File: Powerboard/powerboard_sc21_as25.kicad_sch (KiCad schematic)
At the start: 59 parts, among them J10 Conn_01x04_Male, J2 Conn_01x02_Male, J3 Conn_01x02_Male, J4 Conn_01x08_Male, J9 Conn_Coaxial, Q6 MMDT2222A, Q7 RSJ250P10TL, Q8 RSJ250P10TL, U1 LTC4412xS6, U2 SN65HVD230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

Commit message: update
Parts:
- removed TP1, TP10, TP11, TP12, TP13, TP2, TP26, TP27, TP3, TP4, TP5, TP6, TP7, TP8, TP9: TestPoint, TestPoint:TestPoint_Pad_D1.0mm, symbol Connector:TestPoint
- added C21: 160pF, Capacitor_SMD:C_0603_1608Metric, symbol Device:C_Small
- C17, C18, C2: value 1uF -> 1μF
- C28: value 220pF -> 220 pF
- R11, R4: value 10k -> 10kΩ
- R19, R21, R6, R8: value 470 -> 470Ω
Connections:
- net GND: now also U3.16 (IO27), C21.1
- net at R22.2, U2.1 (D): now also C21.2
- no-connect marks 22 -> 21

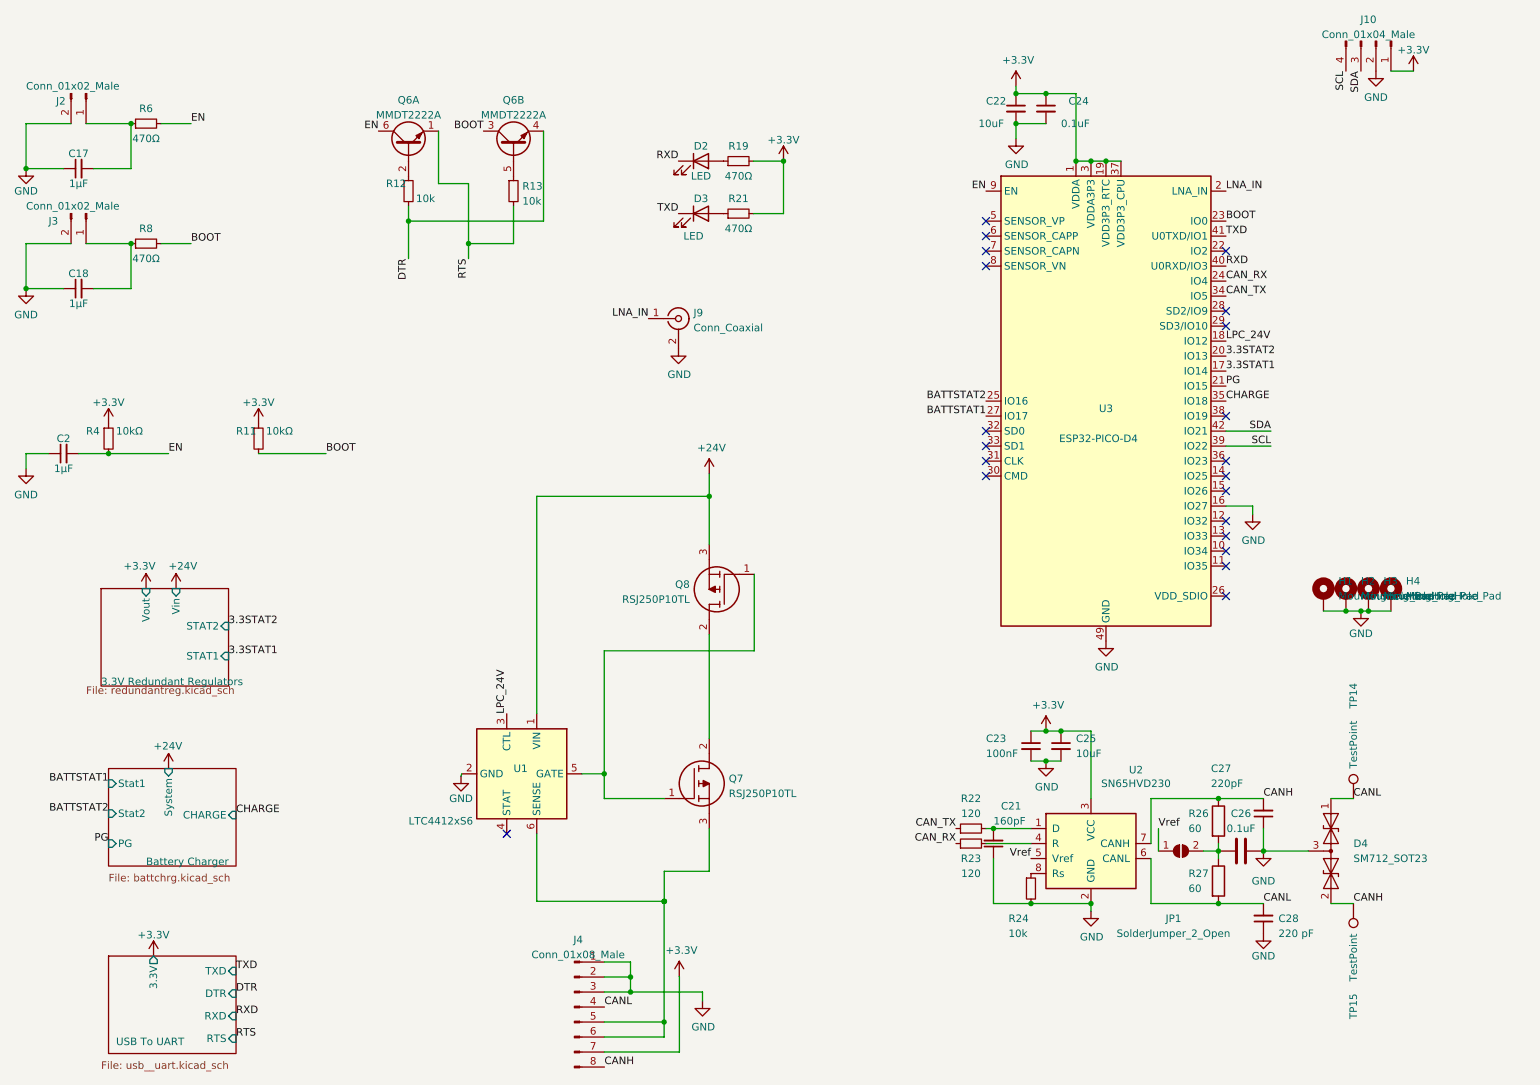
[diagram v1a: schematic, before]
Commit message: Changed some values and footprints since some went out of stock
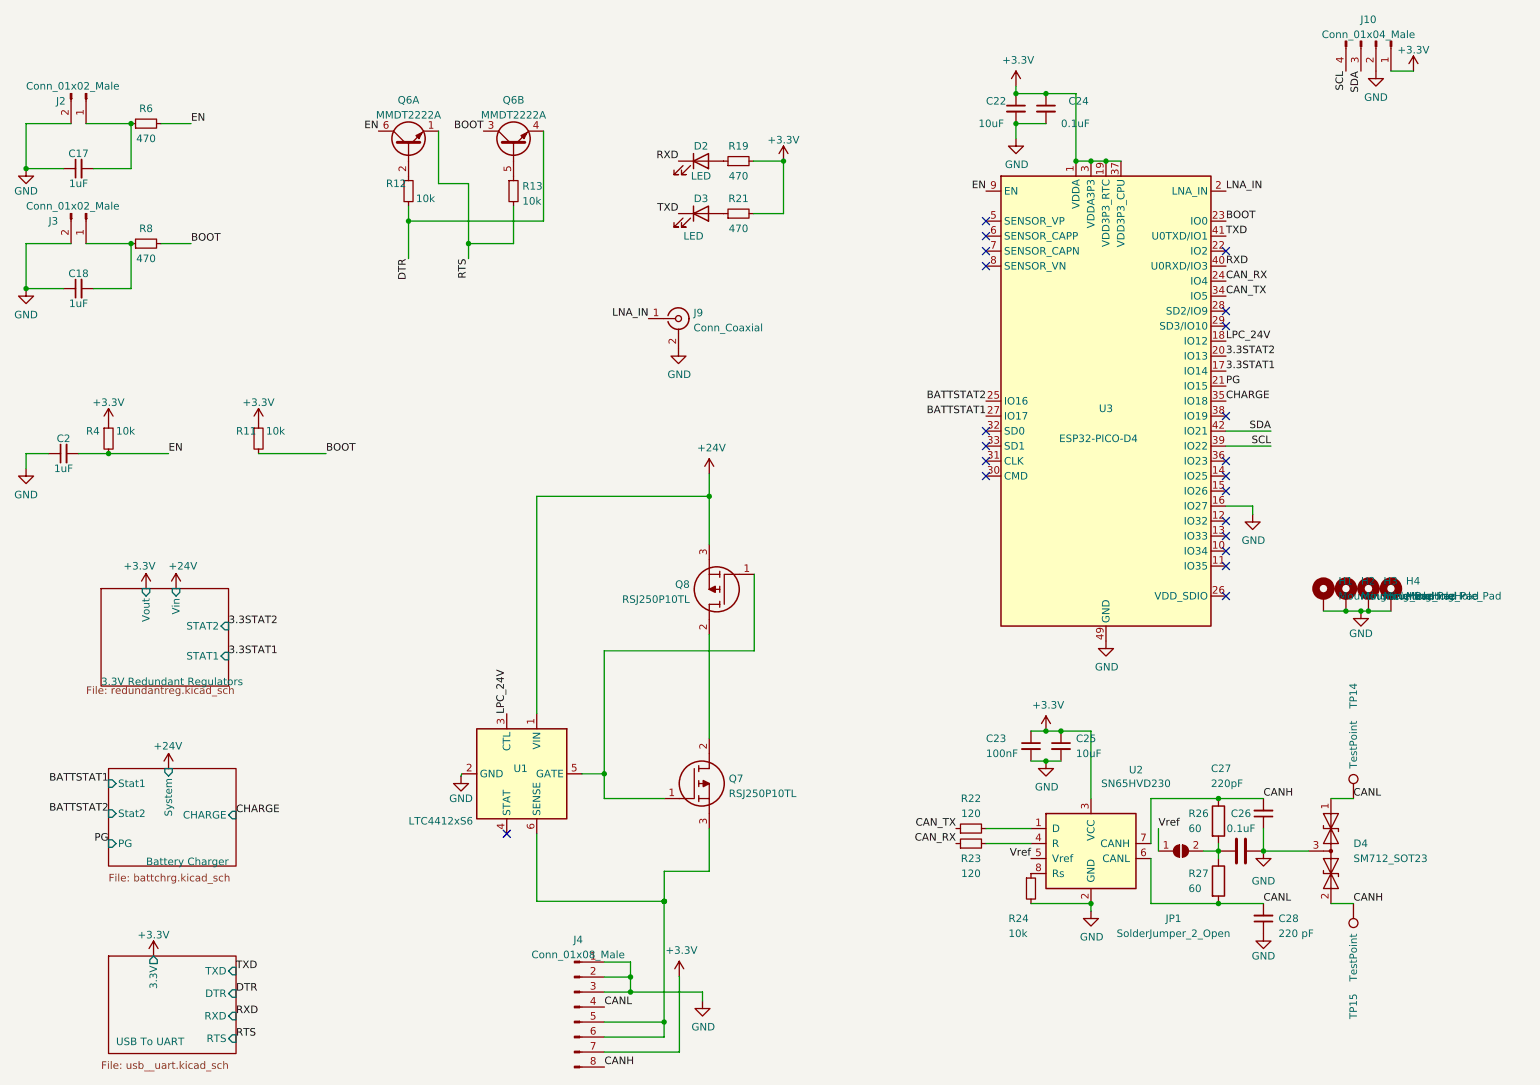
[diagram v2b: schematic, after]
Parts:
- removed C21: 160pF, Capacitor_SMD:C_0603_1608Metric, symbol Device:C_Small
- C17, C18, C2: value 1μF -> 1uF
- R11, R4: value 10kΩ -> 10k
- R19, R21, R6, R8: value 470Ω -> 470

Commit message: update
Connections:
- net LPC_24V: no longer U1.3 (CTL)
- net at Q7.3, U1.6 (SENSE): now also J4.5 (Pin_5), J4.6 (Pin_6)
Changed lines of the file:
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@@
   (junction (at 217.17 33.02) (diameter 0) (color 0 0 0 0)
   )
+  (junction (at 150.0124 146.9644) (diameter 0) (color 0 0 0 0)
+  )
   (junction (at 257.81 109.22) (diameter 0) (color 0 0 0 0)
   )
+  (junction (at 52.07 26.67) (diameter 0) (color 0 0 0 0)
+  )
+  (junction (at 109.22 46.99) (diameter 0) (color 0 0 0 0)
+  )
+  (junction (at 52.07 46.99) (diameter 0) (color 0 0 0 0)
+  )
+  (junction (at 243.84 149.86) (diameter 0) (color 0 0 0 0)
+  )
+  (junction (at 132.207 136.779) (diameter 0) (color 0 0 0 0)
+  )
+  (junction (at 136.652 173.736) (diameter 0) (color 0 0 0 0)
+  )
+  (junction (at 48.26 82.55) (diameter 0) (color 0 0 0 0)
+  )
+  (junction (at 236.22 149.86) (diameter 0) (color 0 0 0 0)
+  )
+  (junction (at 136.652 171.196) (diameter 0) (color 0 0 0 0)
+  )
+  (junction (at 212.09 33.02) (diameter 0) (color 0 0 0 0)
+  )
   (junction (at 142.3416 178.816) (diameter 0) (color 0 0 0 0)
   )
-  (junction (at 52.07 26.67) (diameter 0) (color 0 0 0 0)
-  )
-  (junction (at 109.22 46.99) (diameter 0) (color 0 0 0 0)
-  )
-  (junction (at 52.07 46.99) (diameter 0) (color 0 0 0 0)
-  )
-  (junction (at 142.3924 158.3944) (diameter 0) (color 0 0 0 0)
-  )
-  (junction (at 243.84 149.86) (diameter 0) (color 0 0 0 0)
-  )
-  (junction (at 132.207 136.779) (diameter 0) (color 0 0 0 0)
-  )
-  (junction (at 136.652 173.736) (diameter 0) (color 0 0 0 0)
-  )
-  (junction (at 48.26 82.55) (diameter 0) (color 0 0 0 0)
-  )
-  (junction (at 236.22 149.86) (diameter 0) (color 0 0 0 0)
-  )
-  (junction (at 136.652 171.196) (diameter 0) (color 0 0 0 0)
-  )
-  (junction (at 142.367 158.369) (diameter 0) (color 0 0 0 0)
-  )
-  (junction (at 212.09 33.02) (diameter 0) (color 0 0 0 0)
-  )
   (junction (at 99.06 43.18) (diameter 0) (color 0 0 0 0)
   )
@@
   )
   (junction (at 260.35 109.22) (diameter 0) (color 0 0 0 0)
-  )
-  (junction (at 142.3416 158.3944) (diameter 0) (color 0 0 0 0)
   )
   (junction (at 207.01 129.54) (diameter 0) (color 0 0 0 0)
@@
   (no_connect (at 196.85 45.72))
   (no_connect (at 237.49 88.9))
-  (no_connect (at 115.697 146.939))
+  (no_connect (at 115.7224 146.9644))
   (no_connect (at 237.49 60.96))
   (no_connect (at 237.49 76.2))
@@
     (stroke (width 0) (type default) (color 0 0 0 0))
   )
-  (wire (pts (xy 128.397 136.779) (xy 132.207 136.779))
+  (wire (pts (xy 128.4224 136.8044) (xy 132.207 136.779))
     (stroke (width 0) (type default) (color 0 0 0 0))
   )
@@
     (stroke (width 0) (type default) (color 0 0 0 0))
   )
+  (wire (pts (xy 150.0124 161.4932) (xy 142.3416 161.4932))
+    (stroke (width 0) (type default) (color 0 0 0 0))
+  )
   (wire (pts (xy 99.06 40.64) (xy 99.06 43.18))
     (stroke (width 0) (type default) (color 0 0 0 0))
@@
     (stroke (width 0) (type default) (color 0 0 0 0))
   )
+  (wire (pts (xy 150.0124 146.05) (xy 149.987 146.05))
+    (stroke (width 0) (type default) (color 0 0 0 0))
+  )
   (wire (pts (xy 136.652 171.196) (xy 136.652 173.736))
     (stroke (width 0) (type default) (color 0 0 0 0))
@@
     (stroke (width 0) (type default) (color 0 0 0 0))
   )
-  (wire (pts (xy 142.3416 158.3944) (xy 142.3416 178.816))
-    (stroke (width 0) (type default) (color 0 0 0 0))
-  )
   (wire (pts (xy 44.45 26.67) (xy 52.07 26.67))
     (stroke (width 0) (type default) (color 0 0 0 0))
@@
     (stroke (width 0) (type default) (color 0 0 0 0))
   )
-  (wire (pts (xy 149.987 146.05) (xy 149.987 153.289))
-    (stroke (width 0) (type default) (color 0 0 0 0))
-  )
   (wire (pts (xy 214.63 160.02) (xy 214.63 158.75))
     (stroke (width 0) (type default) (color 0 0 0 0))
@@
     (stroke (width 0) (type default) (color 0 0 0 0))
   )
-  (wire (pts (xy 142.367 158.369) (xy 120.777 158.369))
-    (stroke (width 0) (type default) (color 0 0 0 0))
-  )
   (wire (pts (xy 34.29 34.29) (xy 40.64 34.29))
     (stroke (width 0) (type default) (color 0 0 0 0))
@@
     (stroke (width 0) (type default) (color 0 0 0 0))
   )
+  (wire (pts (xy 142.3416 178.816) (xy 142.3416 181.356))
+    (stroke (width 0) (type default) (color 0 0 0 0))
+  )
   (wire (pts (xy 149.987 89.789) (xy 149.987 97.917))
     (stroke (width 0) (type default) (color 0 0 0 0))
@@
     (stroke (width 0) (type default) (color 0 0 0 0))
   )
+  (wire (pts (xy 150.0124 146.9644) (xy 150.0124 161.4932))
+    (stroke (width 0) (type default) (color 0 0 0 0))
+  )
   (wire (pts (xy 243.84 146.05) (xy 243.84 149.86))
     (stroke (width 0) (type default) (color 0 0 0 0))
@@
     (stroke (width 0) (type default) (color 0 0 0 0))
   )
-  (wire (pts (xy 120.777 126.619) (xy 120.777 89.789))
+  (wire (pts (xy 150.0124 146.05) (xy 150.0124 146.9644))
+    (stroke (width 0) (type default) (color 0 0 0 0))
+  )
+  (wire (pts (xy 120.8024 126.6444) (xy 120.777 89.789))
     (stroke (width 0) (type default) (color 0 0 0 0))
   )
@@
     (stroke (width 0) (type default) (color 0 0 0 0))
   )
-  (wire (pts (xy 107.95 137.16) (xy 108.077 136.779))
+  (wire (pts (xy 107.95 137.16) (xy 108.1024 136.8044))
     (stroke (width 0) (type default) (color 0 0 0 0))
   )
@@
     (stroke (width 0) (type default) (color 0 0 0 0))
   )
+  (wire (pts (xy 120.8024 146.9644) (xy 150.0124 146.9644))
+    (stroke (width 0) (type default) (color 0 0 0 0))
+  )
   (wire (pts (xy 226.06 146.05) (xy 226.06 149.86))
     (stroke (width 0) (type default) (color 0 0 0 0))
@@
     (stroke (width 0) (type default) (color 0 0 0 0))
   )
-  (wire (pts (xy 120.777 158.369) (xy 120.777 146.939))
-    (stroke (width 0) (type default) (color 0 0 0 0))
-  )
   (wire (pts (xy 204.47 158.75) (xy 214.63 158.75))
     (stroke (width 0) (type default) (color 0 0 0 0))
@@
     (stroke (width 0) (type default) (color 0 0 0 0))
   )
+  (wire (pts (xy 142.3416 161.4932) (xy 142.3416 178.816))
+    (stroke (width 0) (type default) (color 0 0 0 0))
+  )
   (wire (pts (xy 255.27 158.75) (xy 259.08 158.75))
     (stroke (width 0) (type default) (color 0 0 0 0))
@@
     (stroke (width 0) (type default) (color 0 0 0 0))
   )
-  (wire (pts (xy 142.3924 158.3944) (xy 142.367 158.369))
-    (stroke (width 0) (type default) (color 0 0 0 0))
-  )
   (wire (pts (xy 254 109.22) (xy 257.81 109.22))
     (stroke (width 0) (type default) (color 0 0 0 0))
@@
     (stroke (width 0) (type default) (color 0 0 0 0))
   )
-  (wire (pts (xy 142.3416 178.816) (xy 142.3416 181.356))
-    (stroke (width 0) (type default) (color 0 0 0 0))
-  )
-  (wire (pts (xy 142.367 153.289) (xy 149.987 153.289))
-    (stroke (width 0) (type default) (color 0 0 0 0))
-  )
   (wire (pts (xy 132.207 136.779) (xy 132.207 140.97))
-    (stroke (width 0) (type default) (color 0 0 0 0))
-  )
-  (wire (pts (xy 142.367 153.289) (xy 142.367 158.369))
     (stroke (width 0) (type default) (color 0 0 0 0))
   )
@@
     (pin "1")
   )
-  (symbol (lib_id "Power_Management:LTC4412xS6") (at 118.237 136.779 270) (unit 1)
-    (in_bom yes) (on_board yes)
-    (property "Reference" "U1" (id 0) (at 116.84 135.89 90)
-      (effects (font (size 1.27 1.27)) (justify left))
-    )
-    (property "Value" "LTC4412xS6" (id 1) (at 99.06 144.78 90)
-      (effects (font (size 1.27 1.27)) (justify left))
-    )
-    (property "Footprint" "Package_TO_SOT_SMD:TSOT-23-6" (id 2) (at 109.347 153.289 0)
-      (effects (font (size 1.27 1.27)) hide)
-    )
-    (property "Datasheet" "https://www.analog.com/media/en/technical-documentation/data-sheets/4412fb.pdf" (id 3) (at 113.157 190.119 0)
-      (effects (font (size 1.27 1.27)) hide)
-    )
+  (symbol (lib_id "Power_Management:LTC4412xS6") (at 118.2624 136.8044 270) (unit 1)
+    (in_bom yes) (on_board yes)
+    (property "Reference" "U1" (id 0) (at 116.8654 135.9154 90)
+      (effects (font (size 1.27 1.27)) (justify left))
+    )
+    (property "Value" "LTC4412xS6" (id 1) (at 99.0854 144.8054 90)
+      (effects (font (size 1.27 1.27)) (justify left))
+    )
+    (property "Footprint" "Package_TO_SOT_SMD:TSOT-23-6" (id 2) (at 109.3724 153.3144 0)
+      (effects (font (size 1.27 1.27)) hide)
+    )
+    (property "Datasheet" "https://www.analog.com/media/en/technical-documentation/data-sheets/4412fb.pdf" (id 3) (at 113.1824 190.1444 0)
+      (effects (font (size 1.27 1.27)) hide)
+    )

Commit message: update 2
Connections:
- net LPC_24V: now also U1.3 (CTL)
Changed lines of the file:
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@@
     (effects (font (size 1.27 1.27)) (justify left bottom))
   )
-  (label "LPC_24V" (at 115.697 126.619 90)
+  (label "LPC_24V" (at 115.7224 126.6444 90)
     (effects (font (size 1.27 1.27)) (justify left bottom))
   )
